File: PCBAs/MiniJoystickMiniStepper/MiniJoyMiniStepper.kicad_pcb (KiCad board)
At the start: 2 copper layers, 88.9 x 142.2 mm, 66 parts, among them J0 STEPPER_UNI_5P, J1 STEPPER_UNI_5P, J10 TH_0.1_1x1, J100 TH_0.1_1x1, J101 TH_0.1_1x1, J102 TH_0.1_1x1, J103 TH_0.1_1x1, J104 TH_0.1_1x1, J105 TH_0.1_1x1, J107 TH_0.1_1x1, J11 TH_0.1_1x1, J12 TH_0.1_1x1, J13 TH_0.1_1x1, J14 TH_0.1_1x1, J15 TH_0.1_1x1, J16 TH_0.1_1x1, J2 STEPPER_UNI_5P, J3 STEPPER_UNI_5P, J4 STEPPER_UNI_5P, J5 STEPPER_UNI_5P, J6 STEPPER_UNI_5P, J7 STEPPER_UNI_5P, J8 TH_0.1_1x1, J9 TH_0.1_1x1, U1 MCP3008T-I/SL, U10 ULN2803, U11 STM32F103C8T6_BLUE_PILL, U2 OLED_128x32_I2C, U3 CD74HC595, U4 CD74HC595, U5 CD74HC595, U6 CD74HC595, U7 ULN2803, U8 ULN2803, U9 ULN2803

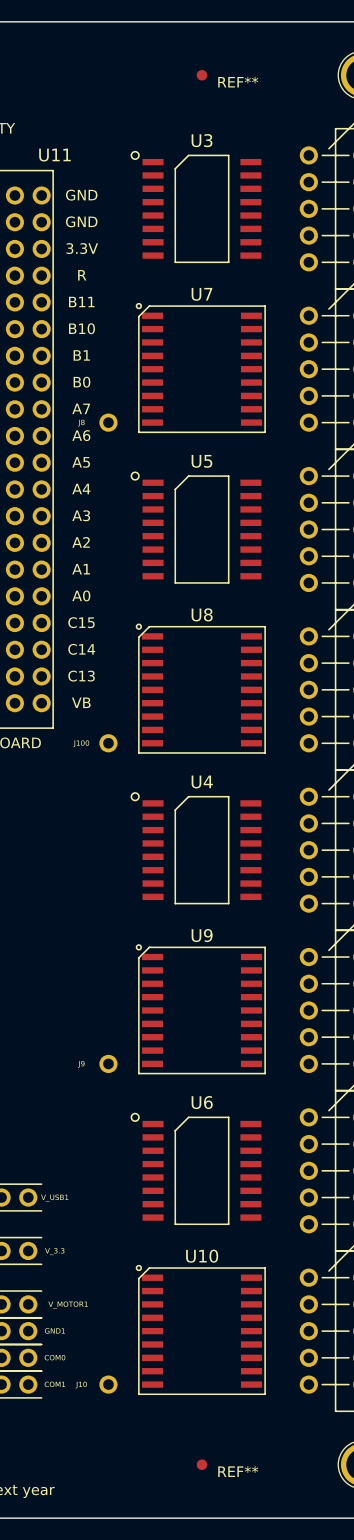
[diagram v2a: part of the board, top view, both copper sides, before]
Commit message: Placed Shift register daisy chain connectors
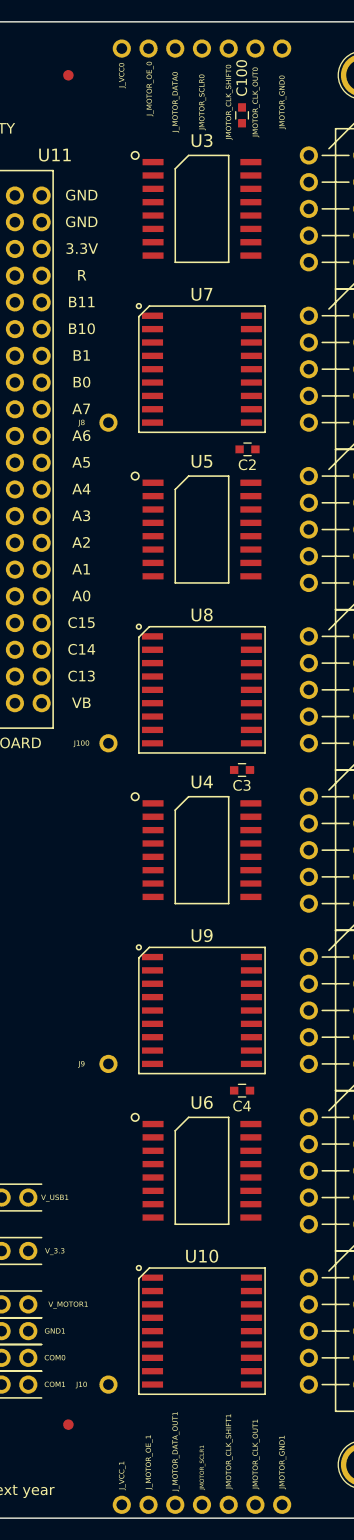
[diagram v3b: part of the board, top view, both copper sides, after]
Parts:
- added C100: 0.1 uF, Capacitors_SMD:C_0603, F.Cu at (174.0, 26.7)
- added C2: 0.1 uF, Capacitors_SMD:C_0603, F.Cu at (174.5, 58.4)
- added C3: 0.1 uF, Capacitors_SMD:C_0603, F.Cu at (174.0, 88.9)
- added C4: 0.1 uF, Capacitors_SMD:C_0603, F.Cu at (174.0, 119.4)
- added JMOTOR_CLK_OUT0: TH_0.1_1x1, Liberry:single_0.1, F.Cu at (175.3, 20.3)
- added JMOTOR_CLK_OUT1: TH_0.1_1x1, Liberry:single_0.1, F.Cu at (175.3, 158.8)
- added JMOTOR_CLK_SHIFT0: TH_0.1_1x1, Liberry:single_0.1, F.Cu at (172.7, 20.3)
- added JMOTOR_CLK_SHIFT1: TH_0.1_1x1, Liberry:single_0.1, F.Cu at (172.7, 158.8)
- added JMOTOR_GND0: TH_0.1_1x1, Liberry:single_0.1, F.Cu at (177.8, 20.3)
- added JMOTOR_GND1: TH_0.1_1x1, Liberry:single_0.1, F.Cu at (177.8, 158.8)
- added JMOTOR_SCLR0: TH_0.1_1x1, Liberry:single_0.1, F.Cu at (170.2, 20.3)
- added JMOTOR_SCLR1: TH_0.1_1x1, Liberry:single_0.1, F.Cu at (170.2, 158.8)
- added J_MOTOR_DATA0: TH_0.1_1x1, Liberry:single_0.1, F.Cu at (167.6, 20.3)
- added J_MOTOR_DATA_OUT1: TH_0.1_1x1, Liberry:single_0.1, F.Cu at (167.6, 158.8)
- added J_MOTOR_OE_0: TH_0.1_1x1, Liberry:single_0.1, F.Cu at (165.1, 20.3)
- added J_MOTOR_OE_1: TH_0.1_1x1, Liberry:single_0.1, F.Cu at (165.1, 158.8)
- added J_VCC0: TH_0.1_1x1, Liberry:single_0.1, F.Cu at (162.6, 20.3)
- added J_VCC_1: TH_0.1_1x1, Liberry:single_0.1, F.Cu at (162.6, 158.8)
- moved REF** 13.3 mm to (157.5, 151.1)
- moved REF** 12.7 mm to (157.5, 22.9)
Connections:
- net /MOTOR_CLK_DATA renamed /MOTOR_CLK_SHIFT

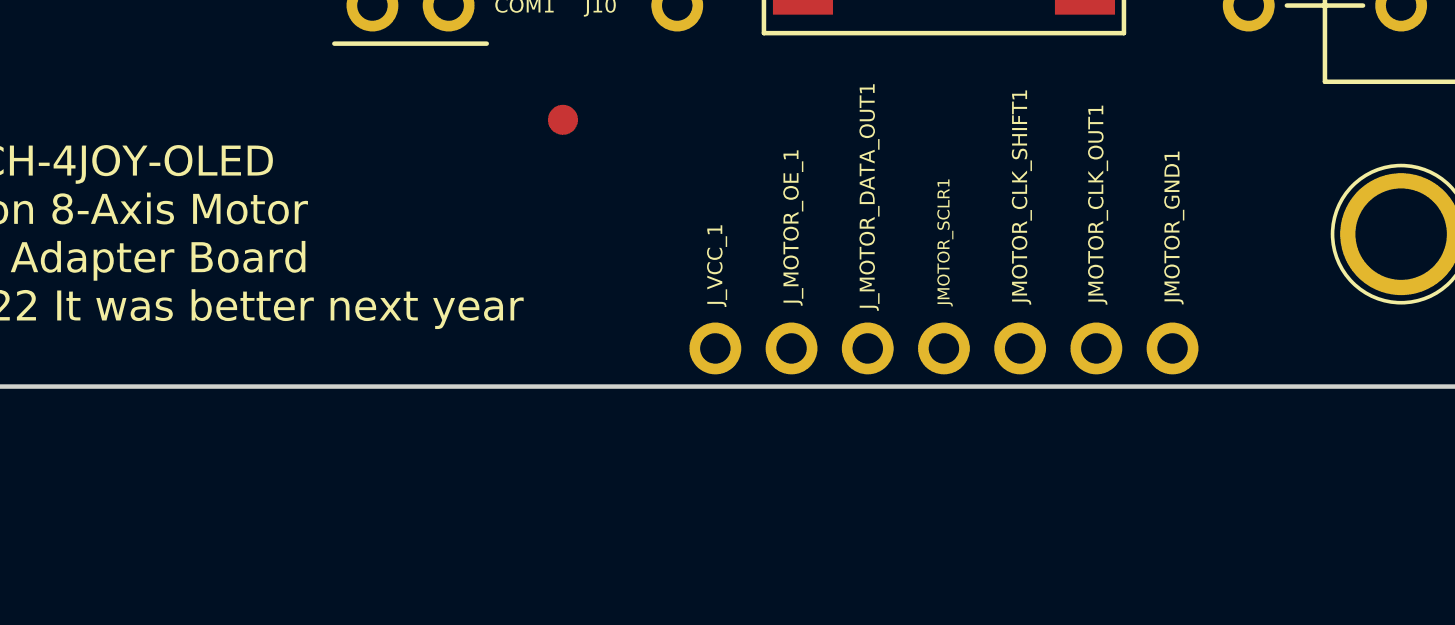
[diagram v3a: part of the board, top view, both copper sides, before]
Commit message: Updated daisy chain. Added extra motor power pins for more current/heat disspation.
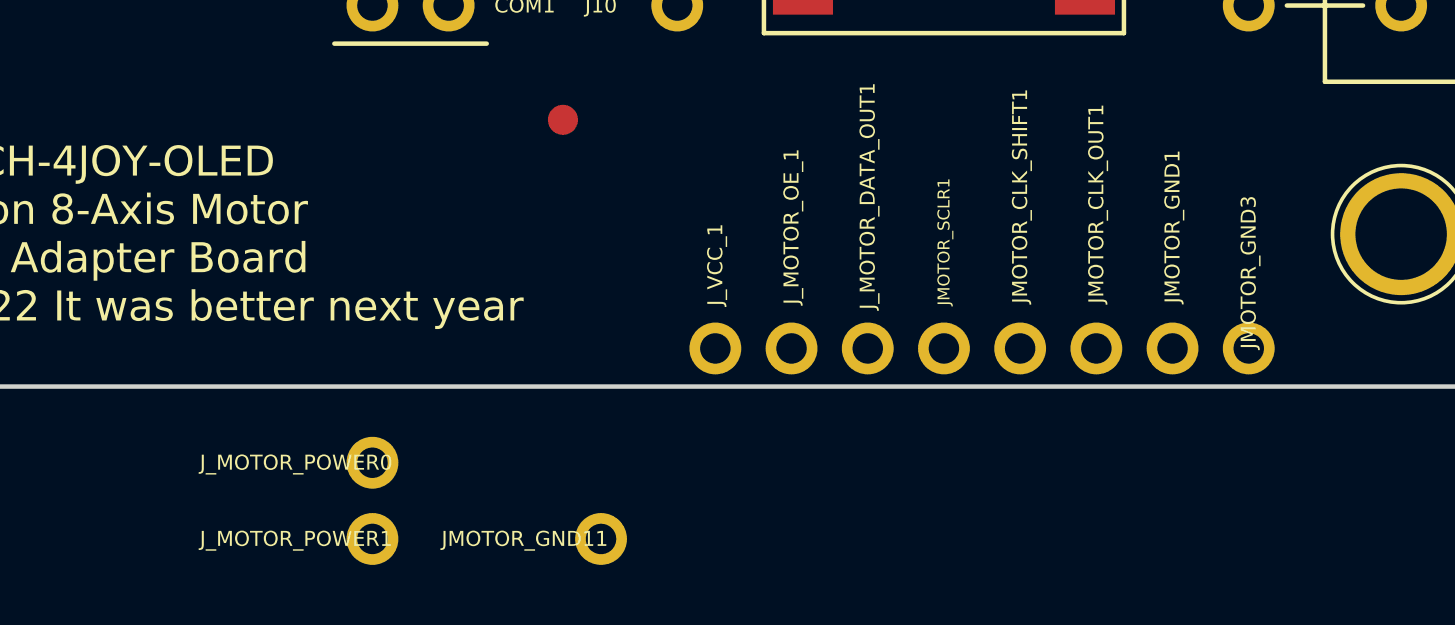
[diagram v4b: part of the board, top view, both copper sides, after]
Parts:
- added JMOTOR_GND11: TH_0.1_1x1, Liberry:single_0.1, F.Cu at (158.8, 165.1)
- added JMOTOR_GND3: TH_0.1_1x1, Liberry:single_0.1, F.Cu at (180.3, 158.8)
- added J_MOTOR_POWER0: TH_0.1_1x1, Liberry:single_0.1, F.Cu at (151.1, 162.6)
- added J_MOTOR_POWER1: TH_0.1_1x1, Liberry:single_0.1, F.Cu at (151.1, 165.1)
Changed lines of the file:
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@@
 (kicad_pcb (version 4) (host pcbnew 4.0.4-stable)
   (general
-    (links 296)
-    (no_connects 296)
+    (links 298)
+    (no_connects 297)
     (area 101.524999 17.704999 190.575001 160.095001)
     (thickness 1.6)
@@
     (tracks 0)
     (zones 0)
-    (modules 84)
-    (nets 125)
+    (modules 88)
+    (nets 127)
   )
   (page A4)
@@
   (net 123 "Net-(J_MOTOR_DATA0-Pad1)")
   (net 124 "Net-(J_MOTOR_OE_0-Pad1)")
+  (net 125 "Net-(J_MOTOR_POWER0-Pad1)")
+  (net 126 "Net-(J_MOTOR_POWER1-Pad1)")
   (net_class Default "This is the default net class."
     (clearance 0.2)
@@
     (add_net "Net-(J_MOTOR_DATA_OUT1-Pad1)")
     (add_net "Net-(J_MOTOR_OE_0-Pad1)")
+    (add_net "Net-(J_MOTOR_POWER0-Pad1)")
+    (add_net "Net-(J_MOTOR_POWER1-Pad1)")
     (add_net "Net-(J_UART1_RX1-Pad1)")
     (add_net "Net-(J_UART1_TX1-Pad1)")
@@
     )
   )
+  (module Liberry:single_0.1 (layer F.Cu)
+    (at 180.34 158.75 270)
+    (descr "10 pins through hole IDC header")
+    (tags "IDC header socket VASCH")
+    (fp_text reference JMOTOR_GND3 (at -2.54 0 270) (layer F.SilkS)
+      (effects (font (size 0.5 0.5) (thickness 0.125)))
+    )
+    (fp_text value TH_0.1_1x1 (at 0 2.54 270) (layer F.Fab)
+      (effects (font (size 1 1) (thickness 0.15)))
+    )
+    (pad 1 thru_hole circle (at 0 0 270) (size 1.7272 1.7272) (drill 1.016) (layers *.Cu *.Mask)
+      (net 11 GND))
+  )
+  (module Liberry:single_0.1 (layer F.Cu)
+    (at 158.75 165.1)
+    (descr "10 pins through hole IDC header")
+    (tags "IDC header socket VASCH")
+    (fp_text reference JMOTOR_GND11 (at -2.54 0) (layer F.SilkS)
+      (effects (font (size 0.5 0.5) (thickness 0.125)))
+    )
+    (fp_text value TH_0.1_1x1 (at 0 2.54) (layer F.Fab)
+      (effects (font (size 1 1) (thickness 0.15)))
+    )
+    (pad 1 thru_hole circle (at 0 0) (size 1.7272 1.7272) (drill 1.016) (layers *.Cu *.Mask)
+      (net 11 GND))
+  )
+  (module Liberry:single_0.1 (layer F.Cu)
+    (at 151.13 162.56)
+    (descr "10 pins through hole IDC header")
+    (tags "IDC header socket VASCH")
+    (fp_text reference J_MOTOR_POWER0 (at -2.54 0) (layer F.SilkS)
+      (effects (font (size 0.5 0.5) (thickness 0.125)))
+    )
+    (fp_text value TH_0.1_1x1 (at 0 2.54) (layer F.Fab)
+      (effects (font (size 1 1) (thickness 0.15)))
+    )
+    (pad 1 thru_hole circle (at 0 0) (size 1.7272 1.7272) (drill 1.016) (layers *.Cu *.Mask)
+      (net 125 "Net-(J_MOTOR_POWER0-Pad1)"))
+  )
+  (module Liberry:single_0.1 (layer F.Cu)
+    (at 151.13 165.1)
+    (descr "10 pins through hole IDC header")
+    (tags "IDC header socket VASCH")
+    (fp_text reference J_MOTOR_POWER1 (at -2.54 0) (layer F.SilkS)
+      (effects (font (size 0.5 0.5) (thickness 0.125)))
+    )
+    (fp_text value TH_0.1_1x1 (at 0 2.54) (layer F.Fab)
+      (effects (font (size 1 1) (thickness 0.15)))
+    )
+    (pad 1 thru_hole circle (at 0 0) (size 1.7272 1.7272) (drill 1.016) (layers *.Cu *.Mask)
+      (net 126 "Net-(J_MOTOR_POWER1-Pad1)"))
+  )
   (gr_line (start 101.6 25.4) (end 101.6 17.78) (layer Edge.Cuts) (width 0.15))

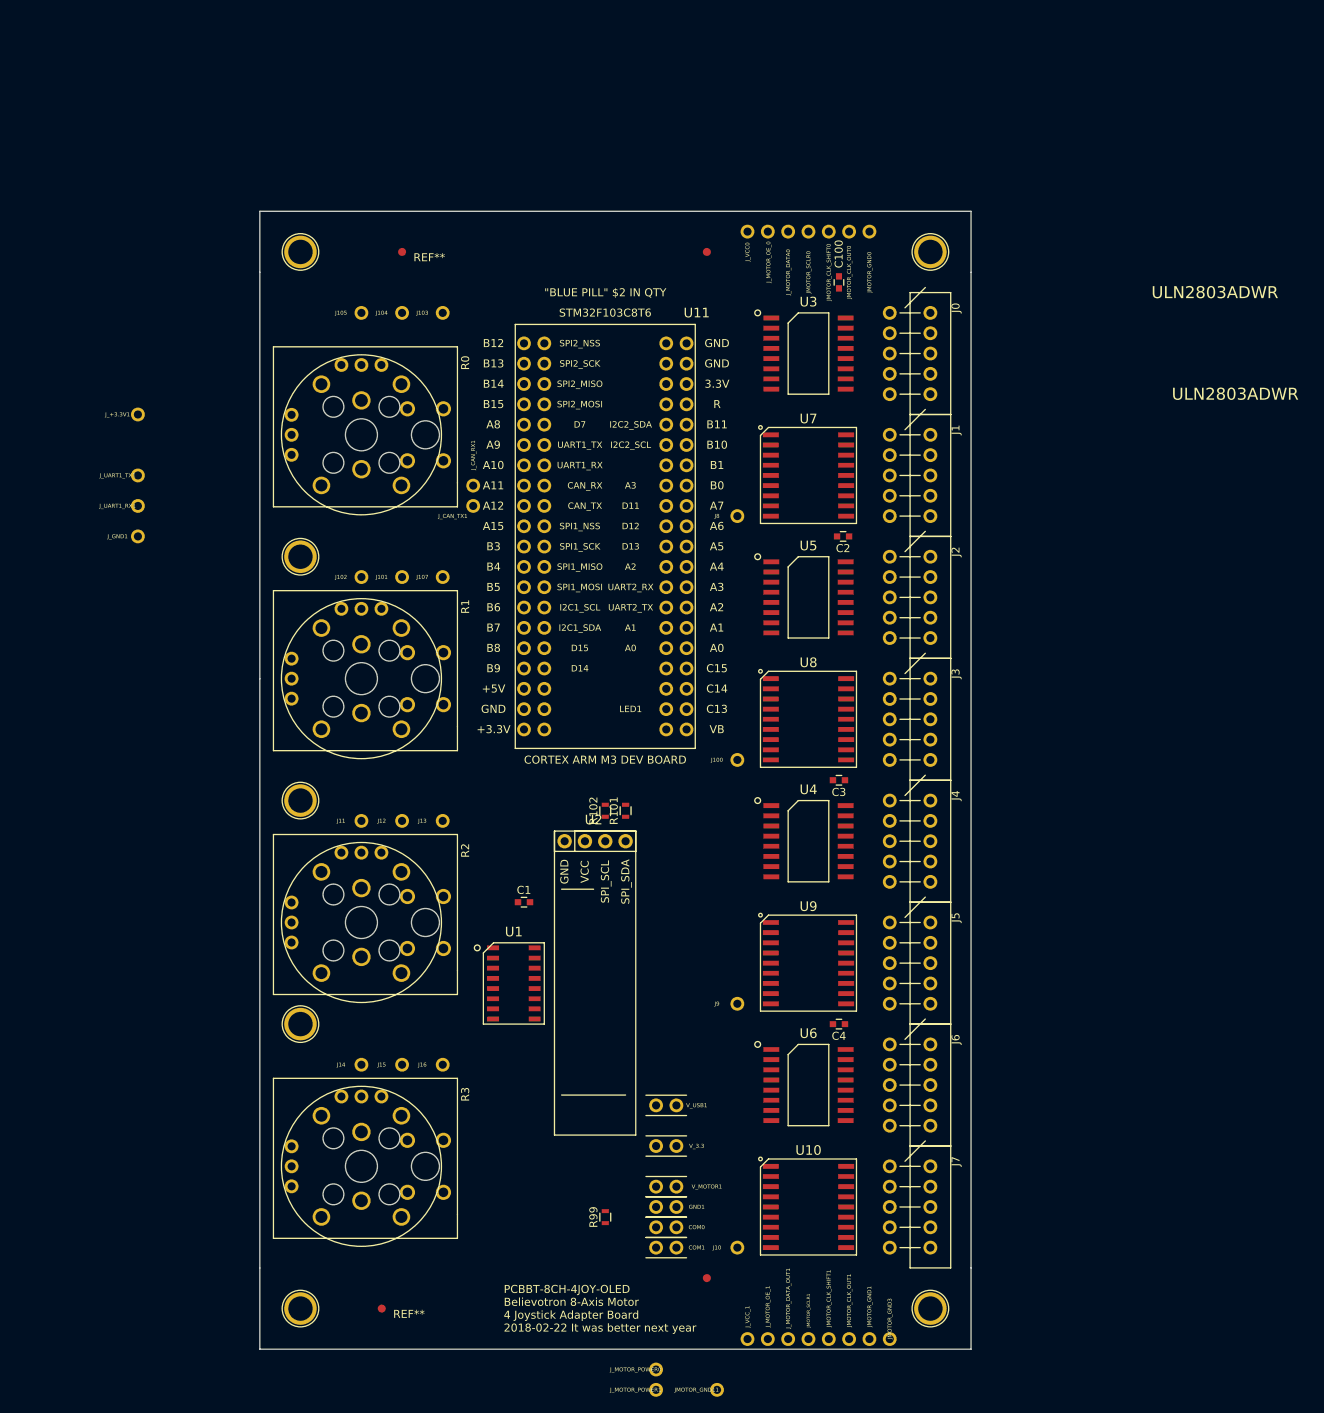
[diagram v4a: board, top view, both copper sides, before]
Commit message: Added FTDI to USB interface. PCB ready for routing
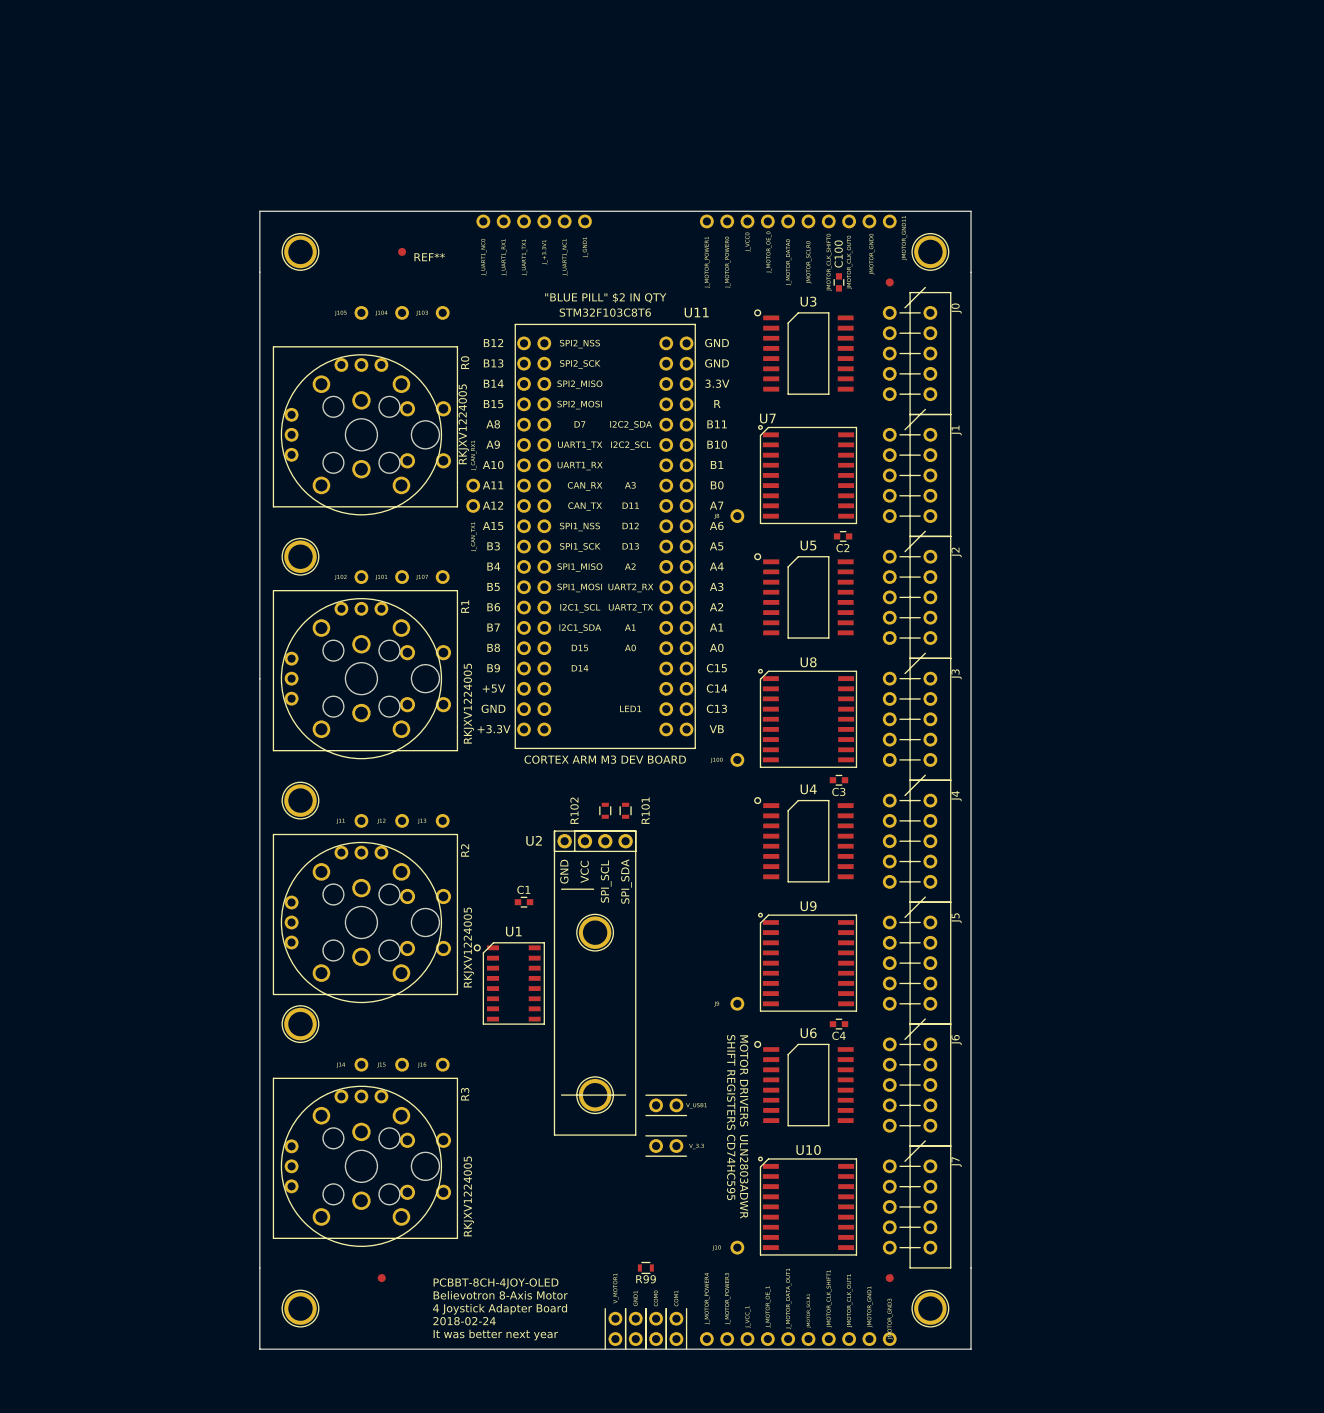
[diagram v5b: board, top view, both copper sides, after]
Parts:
- added J_MOTOR_POWER3: TH_0.1_1x1, Liberry:single_0.1, F.Cu at (160.0, 158.8)
- added J_MOTOR_POWER4: TH_0.1_1x1, Liberry:single_0.1, F.Cu at (157.5, 158.8)
- added J_UART1_NC0: TH_0.1_1x1, Liberry:single_0.1, F.Cu at (129.5, 19.1)
- added J_UART1_NC1: TH_0.1_1x1, Liberry:single_0.1, F.Cu at (139.7, 19.1)
- added REF**: 1pin, Connect:1pin, F.Cu at (143.5, 108.0)
- added REF**: 1pin, Connect:1pin, F.Cu at (143.5, 128.3)
- moved JMOTOR_GND11 147.6 mm to (180.3, 19.1), turned to 90 degrees
- moved J_MOTOR_POWER1 146.2 mm to (157.5, 19.1), turned to 90 degrees
- moved J_MOTOR_POWER0 143.8 mm to (160.0, 19.1), turned to 90 degrees
- moved J_GND1 68.4 mm to (142.2, 19.1), turned to 90 degrees
- moved J_UART1_RX1 57.9 mm to (132.1, 19.1), turned to 90 degrees
- moved J_UART1_TX1 57.8 mm to (134.6, 19.1), turned to 90 degrees
- moved J_+3.3V1 56.2 mm to (137.2, 19.1), turned to 90 degrees
- moved REF** 23.2 mm to (180.3, 26.7)
- moved REF** 22.9 mm to (180.3, 151.1)
- moved V_MOTOR1 18.2 mm to (146.1, 156.2), turned to 270 degrees
- moved GND1 14.9 mm to (148.6, 156.2), turned to 270 degrees
- moved COM0 11.7 mm to (151.1, 156.2), turned to 270 degrees
- moved COM1 8.89 mm to (153.7, 156.2), turned to 270 degrees
- moved R99 8.13 mm to (149.9, 149.9), turned to 180 degrees
- moved REF** 3.81 mm to (116.8, 151.1)
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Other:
- board text added: "MOTOR DRIVERS ULN2803ADWR SHIFT REGISTERS CD74HC595"
- board text added: "PCBBT-8CH-4JOY-OLED Believotron 8-Axis Motor 4 Joystick Adapter Board 2018-02-24 It was better next year"
- board text added: "RKJXV1224005"
- board text removed: "PCBBT-8CH-4JOY-OLED Believotron 8-Axis Motor 4 Joystick Adapter Board 2018-02-22 It was better next year"
- board text removed: "ULN2803ADWR"
